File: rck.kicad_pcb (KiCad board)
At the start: 2 copper layers, 142.3 x 183.9 mm, 40 parts, among them J01 Conn_02x22_Row_Letter_Last, J02 Conn_02x22_Row_Letter_Last, J03 Conn_02x22_Row_Letter_Last, J04 Conn_02x22_Row_Letter_Last

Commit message: V1.0Rack
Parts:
- added J5: Conn_01x02_Pin, Connector_PinHeader_2.54mm:PinHeader_1x02_P2.54mm_Vertical, F.Cu at (148.8, 18.7)
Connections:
- J01 pad 22a: unconnected-(J01-Pin_22a-Pad22a) -> GND
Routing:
- net Net-(J01-Pin_15a): track 257.7 -> 246.1 mm
- net Net-(J01-Pin_4a): track 138.4 -> 127.4 mm
- net Net-(J01-Pin_16a): track 241.7 -> 231.1 mm
- net VCC: track 396.5 -> 406.6 mm
- net Net-(J01-Pin_14a): track 282.7 -> 272.9 mm
- net Net-(J01-Pin_17a): track 263.7 -> 254.3 mm
- net Net-(J01-Pin_5a): track 139.0 -> 131.7 mm
- net Net-(J01-Pin_18a): track 241.5 -> 234.9 mm
- net Net-(J01-Pin_6a): track 138.2 -> 132.2 mm
- net Net-(J01-Pin_7a): track 133.5 -> 127.6 mm
- net Net-(J01-Pin_3a): track 138.1 -> 134.0 mm
- net Net-(J01-Pin_11a): track 195.8 -> 197.8 mm
- net Net-(J01-Pin_12a): track 189.5 -> 191.0 mm
- net Net-(J01-Pin_13a): track 190.0 -> 189.0 mm
- added copper zone on B.Cu, net GND
- added copper zone on F.Cu, net GND
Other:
- board size 142.3 x 183.9 mm -> 130 x 184 mm
- board text added: "F1"
- board text added: "F2"
- board text added: "F3"
- board text added: "F4"
- board text added: "F5"
- board text added: "F6"

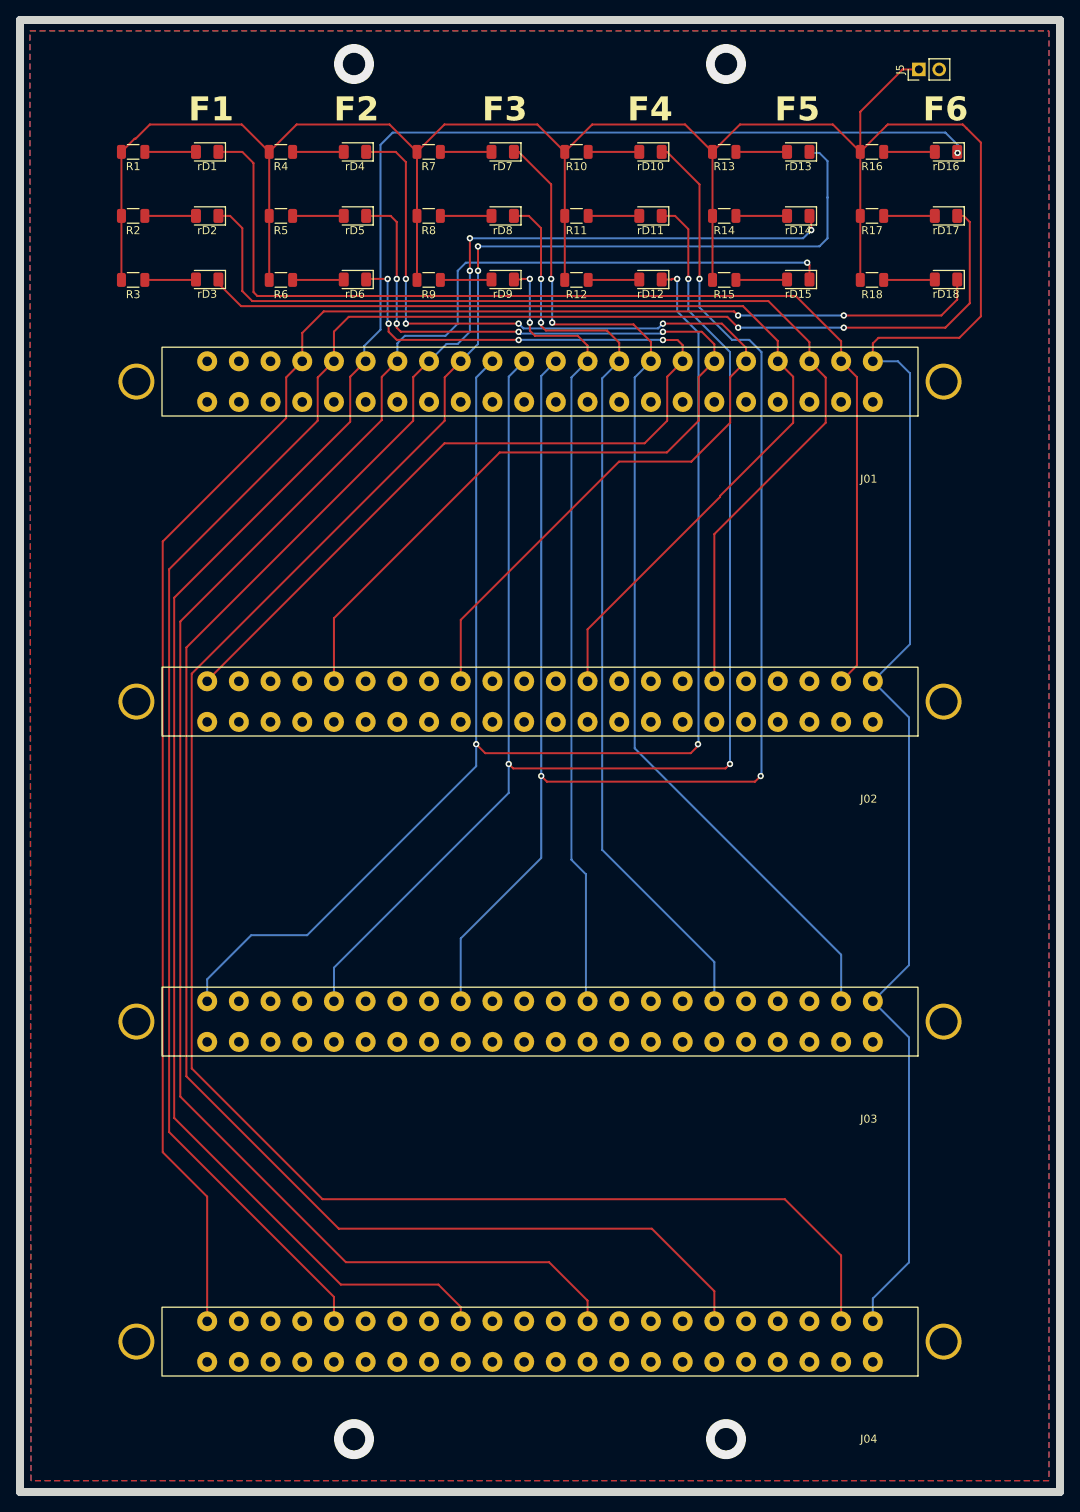
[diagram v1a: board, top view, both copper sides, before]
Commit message: v2Reg12v
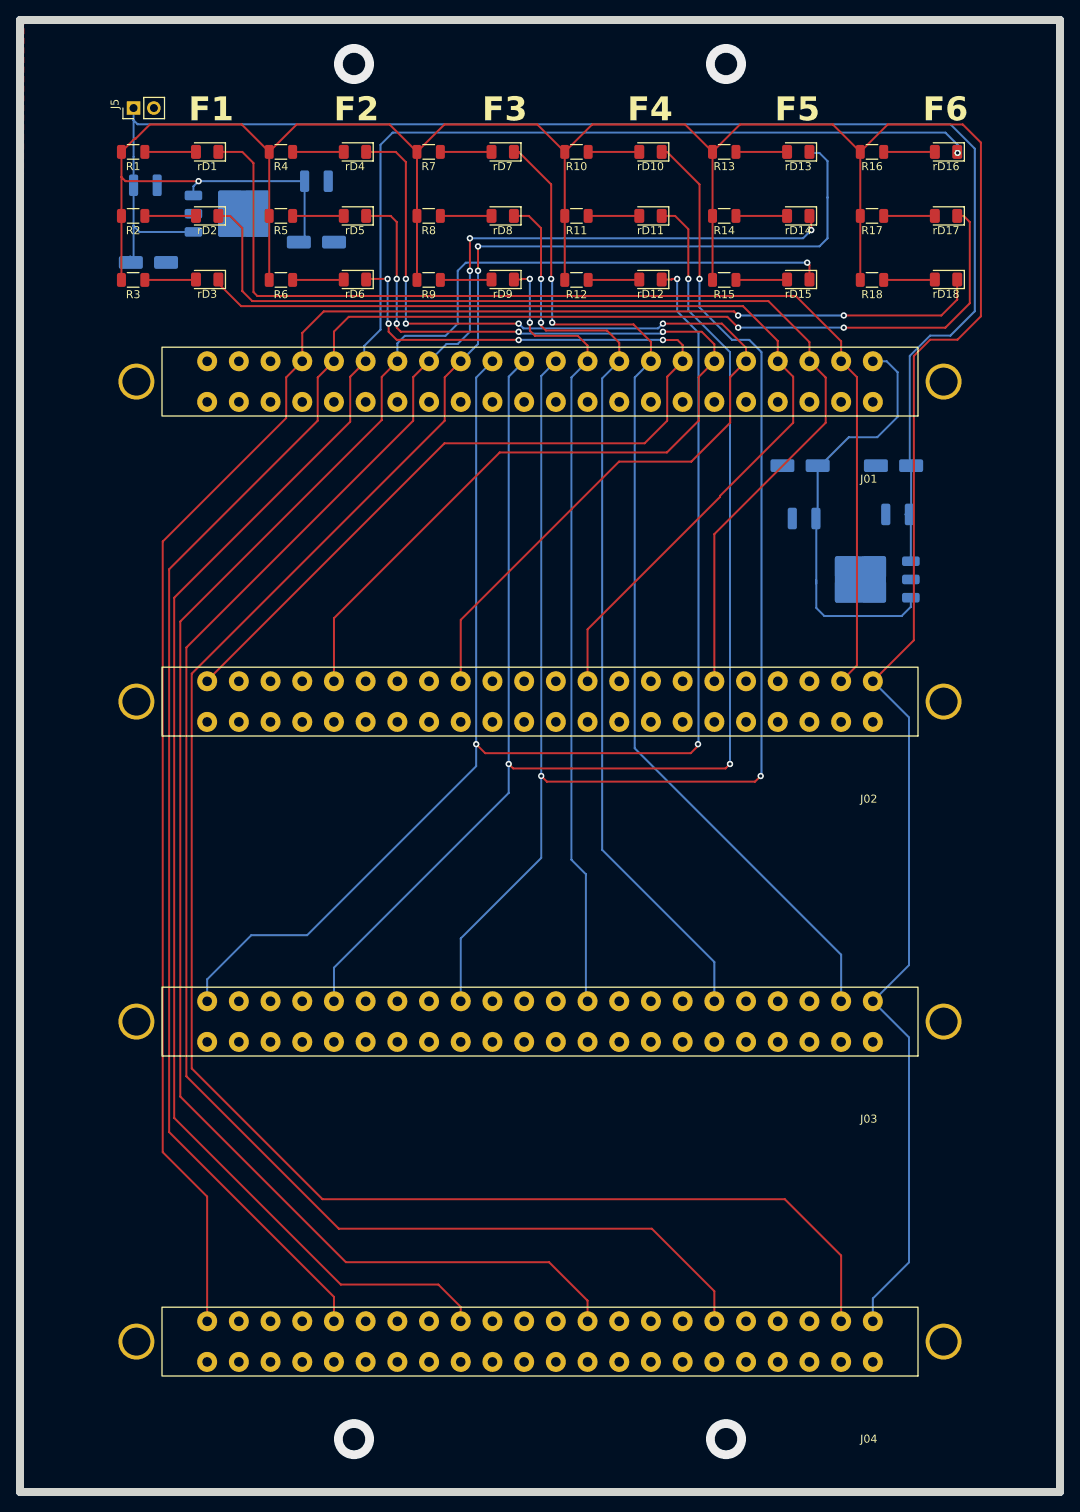
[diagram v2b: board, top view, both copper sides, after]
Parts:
- added C1: Cap Pol1, Capacitor_SMD:CP_Elec_5x5.9, B.Cu at (52.5, 42.8)
- added C2: Cap, Capacitor_SMD:C_1210_3225Metric, B.Cu at (52.1, 33.1)
- added C3: Cap Pol1, Capacitor_SMD:CP_Elec_5x5.9, B.Cu at (73.5, 40.2)
- added C4: Cap, Capacitor_SMD:C_1210_3225Metric, B.Cu at (73.5, 32.6)
- added C5: Cap Pol1, Capacitor_SMD:CP_Elec_5x5.9, B.Cu at (145.6, 68.2)
- added C6: Cap, Capacitor_SMD:C_1210_3225Metric, B.Cu at (146.1, 74.3)
- added C7: Cap Pol1, Capacitor_SMD:CP_Elec_5x5.9, B.Cu at (134.0, 68.2)
- added C8: Cap, Capacitor_SMD:C_1210_3225Metric, B.Cu at (134.5, 74.8)
- added VR1: Volt Reg, Package_TO_SOT_SMD:TO-252-3_TabPin2, B.Cu at (63.2, 36.7)
- added VR2: Volt Reg, Package_TO_SOT_SMD:TO-252-3_TabPin2, B.Cu at (142.8, 82.4)
- moved J5 98.3 mm to (50.6, 23.5)
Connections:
- J01 pad 1a: VCC -> +5V
- J5 pad 1: VCC -> +12V
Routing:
- net +12V: track 0.00 -> 193.6 mm
- net +5V: track 0.00 -> 53.7 mm
- net VCC: track 406.6 -> 415.5 mm, vias 0 -> 1

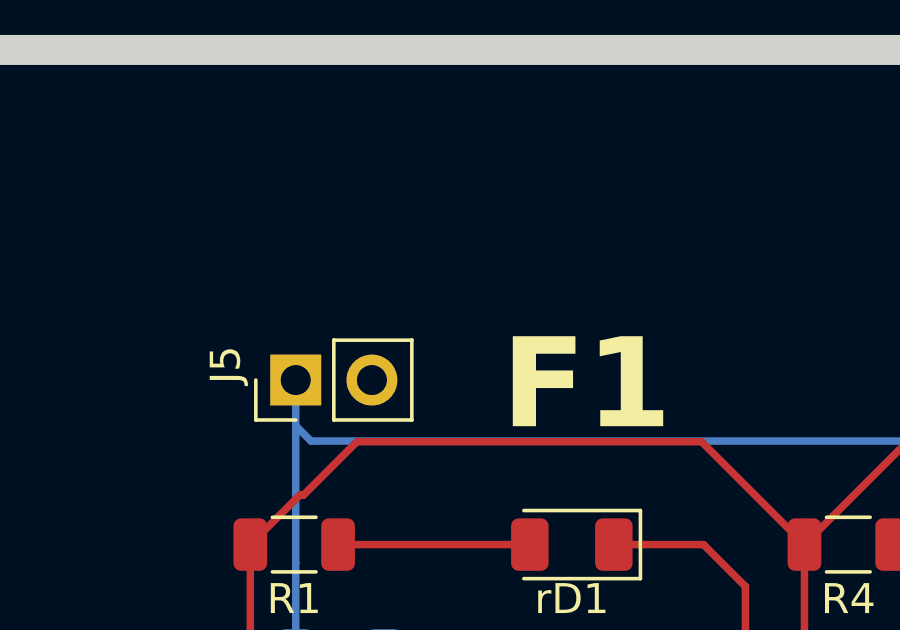
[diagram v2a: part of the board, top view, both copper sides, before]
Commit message: v2Reg12vMolex
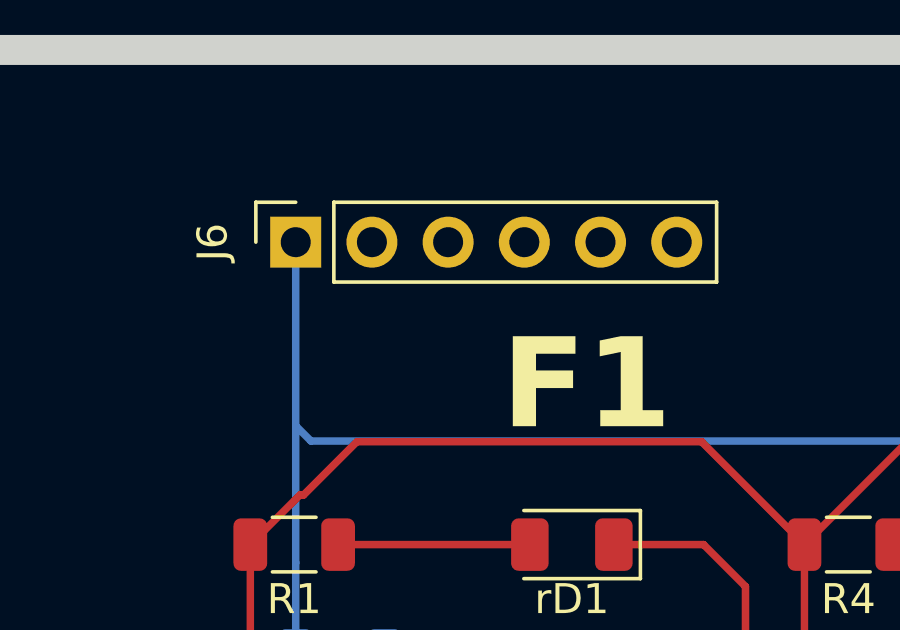
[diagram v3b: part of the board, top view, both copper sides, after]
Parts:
- removed J5: Conn_01x02_Pin, Connector_PinHeader_2.54mm:PinHeader_1x02_P2.54mm_Vertical
- added J6: Conn_01x06_Pin, Connector_PinSocket_2.54mm:PinSocket_1x06_P2.54mm_Vertical, F.Cu at (50.6, 18.9)
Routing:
- net +12V: track 193.6 -> 198.2 mm
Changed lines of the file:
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@@
   (net 174 "+12V")
   (net 175 "+5V")
+  (net 176 "unconnected-(J6-Pin_5-Pad5)")
+  (net 177 "unconnected-(J6-Pin_6-Pad6)")
+  (net 178 "unconnected-(J6-Pin_3-Pad3)")
+  (net 179 "unconnected-(J6-Pin_4-Pad4)")
   (footprint "Resistor_SMD:R_1206_3216Metric" (layer "F.Cu")
     (at 142.94682 44.963 180)
@@
     )
   )
-  (footprint "Connector_PinHeader_2.54mm:PinHeader_1x02_P2.54mm_Vertical" (layer "F.Cu")
-    (at 50.64146 23.477 90)
-    (descr "Through hole straight pin header, 1x02, 2.54mm pitch, single row")
-    (tags "Through hole pin header THT 1x02 2.54mm single row")
-    (property "Sheetfile" "rck.kicad_sch")
-    (property "Sheetname" "")
-    (property "ki_description" "Generic connector, single row, 01x02, script generated")
-    (property "ki_keywords" "connector")
-    (attr through_hole)
-    (fp_text reference "J5" (at 0.508 -2.33 90) (layer "F.SilkS")
-        (effects (font (size 1 1) (thickness 0.15)))
-    )
-    (fp_text value "Conn_01x02_Pin" (at 0 4.87 90) (layer "F.Fab")
-        (effects (font (size 1 1) (thickness 0.15)))
-    )
-    (fp_text user "${REFERENCE}" (at 0.508 1.27) (layer "F.Fab")
-        (effects (font (size 1 1) (thickness 0.15)))
-    )
-    (fp_line (start -1.33 -1.33) (end 0 -1.33)
-      (stroke (width 0.12) (type solid)) (layer "F.SilkS"))
-    (fp_line (start -1.33 0) (end -1.33 -1.33)
-      (stroke (width 0.12) (type solid)) (layer "F.SilkS"))
-    (fp_line (start -1.33 1.27) (end -1.33 3.87)
-      (stroke (width 0.12) (type solid)) (layer "F.SilkS"))
-    (fp_line (start -1.33 1.27) (end 1.33 1.27)
-      (stroke (width 0.12) (type solid)) (layer "F.SilkS"))
-    (fp_line (start -1.33 3.87) (end 1.33 3.87)
-      (stroke (width 0.12) (type solid)) (layer "F.SilkS"))
-    (fp_line (start 1.33 1.27) (end 1.33 3.87)
-      (stroke (width 0.12) (type solid)) (layer "F.SilkS"))
-    (fp_line (start -1.8 -1.8) (end -1.8 4.35)
-      (stroke (width 0.05) (type solid)) (layer "F.CrtYd"))
-    (fp_line (start -1.8 4.35) (end 1.8 4.35)
-      (stroke (width 0.05) (type solid)) (layer "F.CrtYd"))
-    (fp_line (start 1.8 -1.8) (end -1.8 -1.8)
-      (stroke (width 0.05) (type solid)) (layer "F.CrtYd"))
-    (fp_line (start 1.8 4.35) (end 1.8 -1.8)
-      (stroke (width 0.05) (type solid)) (layer "F.CrtYd"))
-    (fp_line (start -1.27 -0.635) (end -0.635 -1.27)
-      (stroke (width 0.1) (type solid)) (layer "F.Fab"))
-    (fp_line (start -1.27 3.81) (end -1.27 -0.635)
-      (stroke (width 0.1) (type solid)) (layer "F.Fab"))
-    (fp_line (start -0.635 -1.27) (end 1.27 -1.27)
-      (stroke (width 0.1) (type solid)) (layer "F.Fab"))
-    (fp_line (start 1.27 -1.27) (end 1.27 3.81)
-      (stroke (width 0.1) (type solid)) (layer "F.Fab"))
-    (fp_line (start 1.27 3.81) (end -1.27 3.81)
-      (stroke (width 0.1) (type solid)) (layer "F.Fab"))
-    (pad "1" thru_hole rect (at 0 0 90) (size 1.7 1.7) (drill 1) (layers "*.Cu" "*.Mask")
-      (net 174 "+12V") (pinfunction "Pin_1") (pintype "passive"))
-    (pad "2" thru_hole oval (at 0 2.54 90) (size 1.7 1.7) (drill 1) (layers "*.Cu" "*.Mask")
-      (net 43 "GND") (pinfunction "Pin_2") (pintype "passive"))
-    (model "${KICAD6_3DMODEL_DIR}/Connector_PinHeader_2.54mm.3dshapes/PinHeader_1x02_P2.54mm_Vertical.wrl"
-      (offset (xyz 0 0 0))
-      (scale (xyz 1 1 1))
-      (rotate (xyz 0 0 0))
-    )
-  )
   (footprint "LED_SMD:LED_1206_3216Metric" (layer "F.Cu")
     (at 133.731184 44.913 180)
@@
     )
   )
+  (footprint "Connector_PinSocket_2.54mm:PinSocket_1x06_P2.54mm_Vertical" (layer "F.Cu")
+    (at 50.64146 18.88 90)
+    (descr "Through hole straight socket strip, 1x06, 2.54mm pitch, single row (from Kicad 4.0.7), script generated")
+    (tags "Through hole socket strip THT 1x06 2.54mm single row")
+    (property "Sheetfile" "rck.kicad_sch")
+    (property "Sheetname" "")
+    (property "ki_description" "Generic connector, single row, 01x06, script generated")
+    (property "ki_keywords" "connector")
+    (attr through_hole)
+    (fp_text reference "J6" (at 0 -2.77 90) (layer "F.SilkS")
+        (effects (font (size 1 1) (thickness 0.15)))
+    )
+    (fp_text value "Conn_01x06_Pin" (at 0 15.47 90) (layer "F.Fab")
+        (effects (font (size 1 1) (thickness 0.15)))
+    )
+    (fp_text user "${REFERENCE}" (at 0 6.35) (layer "F.Fab")
+        (effects (font (size 1 1) (thickness 0.15)))
+    )
+    (fp_line (start -1.33 1.27) (end -1.33 14.03)
+      (stroke (width 0.12) (type solid)) (layer "F.SilkS"))
+    (fp_line (start -1.33 1.27) (end 1.33 1.27)
+      (stroke (width 0.12) (type solid)) (layer "F.SilkS"))
+    (fp_line (start -1.33 14.03) (end 1.33 14.03)
+      (stroke (width 0.12) (type solid)) (layer "F.SilkS"))
+    (fp_line (start 0 -1.33) (end 1.33 -1.33)
+      (stroke (width 0.12) (type solid)) (layer "F.SilkS"))
+    (fp_line (start 1.33 -1.33) (end 1.33 0)
+      (stroke (width 0.12) (type solid)) (layer "F.SilkS"))
+    (fp_line (start 1.33 1.27) (end 1.33 14.03)
+      (stroke (width 0.12) (type solid)) (layer "F.SilkS"))
+    (fp_line (start -1.8 -1.8) (end 1.75 -1.8)
+      (stroke (width 0.05) (type solid)) (layer "F.CrtYd"))
+    (fp_line (start -1.8 14.45) (end -1.8 -1.8)
+      (stroke (width 0.05) (type solid)) (layer "F.CrtYd"))
+    (fp_line (start 1.75 -1.8) (end 1.75 14.45)
+      (stroke (width 0.05) (type solid)) (layer "F.CrtYd"))
+    (fp_line (start 1.75 14.45) (end -1.8 14.45)
+      (stroke (width 0.05) (type solid)) (layer "F.CrtYd"))
+    (fp_line (start -1.27 -1.27) (end 0.635 -1.27)
+      (stroke (width 0.1) (type solid)) (layer "F.Fab"))
+    (fp_line (start -1.27 13.97) (end -1.27 -1.27)
+      (stroke (width 0.1) (type solid)) (layer "F.Fab"))
+    (fp_line (start 0.635 -1.27) (end 1.27 -0.635)
+      (stroke (width 0.1) (type solid)) (layer "F.Fab"))
+    (fp_line (start 1.27 -0.635) (end 1.27 13.97)
+      (stroke (width 0.1) (type solid)) (layer "F.Fab"))
+    (fp_line (start 1.27 13.97) (end -1.27 13.97)
+      (stroke (width 0.1) (type solid)) (layer "F.Fab"))
+    (pad "1" thru_hole rect (at 0 0 90) (size 1.7 1.7) (drill 1) (layers "*.Cu" "*.Mask")
+      (net 174 "+12V") (pinfunction "Pin_1") (pintype "passive"))
+    (pad "2" thru_hole oval (at 0 2.54 90) (size 1.7 1.7) (drill 1) (layers "*.Cu" "*.Mask")
+      (net 43 "GND") (pinfunction "Pin_2") (pintype "passive"))
+    (pad "3" thru_hole oval (at 0 5.08 90) (size 1.7 1.7) (drill 1) (layers "*.Cu" "*.Mask")
+      (net 178 "unconnected-(J6-Pin_3-Pad3)") (pinfunction "Pin_3") (pintype "passive"))
+    (pad "4" thru_hole oval (at 0 7.62 90) (size 1.7 1.7) (drill 1) (layers "*.Cu" "*.Mask")
+      (net 179 "unconnected-(J6-Pin_4-Pad4)") (pinfunction "Pin_4") (pintype "passive"))
+    (pad "5" thru_hole oval (at 0 10.16 90) (size 1.7 1.7) (drill 1) (layers "*.Cu" "*.Mask")
+      (net 176 "unconnected-(J6-Pin_5-Pad5)") (pinfunction "Pin_5") (pintype "passive"))
+    (pad "6" thru_hole oval (at 0 12.7 90) (size 1.7 1.7) (drill 1) (layers "*.Cu" "*.Mask")
+      (net 177 "unconnected-(J6-Pin_6-Pad6)") (pinfunction "Pin_6") (pintype "passive"))
+    (model "${KICAD6_3DMODEL_DIR}/Connector_PinSocket_2.54mm.3dshapes/PinSocket_1x06_P2.54mm_Vertical.wrl"
+      (offset (xyz 0 0 0))
+      (scale (xyz 1 1 1))
+      (rotate (xyz 0 0 0))
+    )
+  )
   (footprint "LED_SMD:LED_1206_3216Metric" (layer "F.Cu")
     (at 59.846096 28.961 180)
@@
   (segment (start 50.64146 42.445) (end 50.30546 42.781) (width 0.25) (layer "B.Cu") (net 174))
   (segment (start 50.23146 42.007) (end 49.45746 42.781) (width 0.25) (layer "B.Cu") (net 174))
+  (segment (start 50.64146 25.001) (end 50.64146 18.88) (width 0.25) (layer "B.Cu") (net 174))
   (segment (start 155.79746 28.557) (end 152.74946 25.509) (width 0.25) (layer "B.Cu") (net 174))
   (segment (start 50.64146 29.573) (end 50.64146 25.001) (width 0.25) (layer "B.Cu") (net 174))
-  (segment (start 50.64146 25.001) (end 50.64146 23.477) (width 0.25) (layer "B.Cu") (net 174))
   (segment (start 150.20946 51.925) (end 152.74946 51.925) (width 0.25) (layer "B.Cu") (net 174))
   (segment (start 50.64146 38.209) (end 50.64146 42.445) (width 0.25) (layer "B.Cu") (net 174))

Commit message: corrección5V
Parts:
- VR2: footprint Package_TO_SOT_SMD:TO-252-3_TabPin2 -> Package_TO_SOT_SMD:TO-263-2
- moved VR2 3.10 mm to (140.3, 84.2)
- moved C8 1.79 mm to (132.7, 74.5)
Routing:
- net +5V: track 53.7 -> 67.4 mm
- net +12V: track 198.2 -> 200.1 mm
- net VCC: track 415.5 -> 416.7 mm
- net Net-(J01-Pin_14a): track 272.9 -> 273.2 mm, vias 2 -> 3
